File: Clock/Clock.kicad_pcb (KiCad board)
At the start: 2 copper layers, 85 x 100 mm, 49 parts, among them J1 LED, J2 BUS LEDs, J3 USB_B_Micro, SW1 Pulse, SW2 SW_SPDT, SW3 Reset, U1 TLC555xP, U2 TLC555xP, U3 TLC555xP, U4 74HC14, U5 74LS08, U6 74LS32

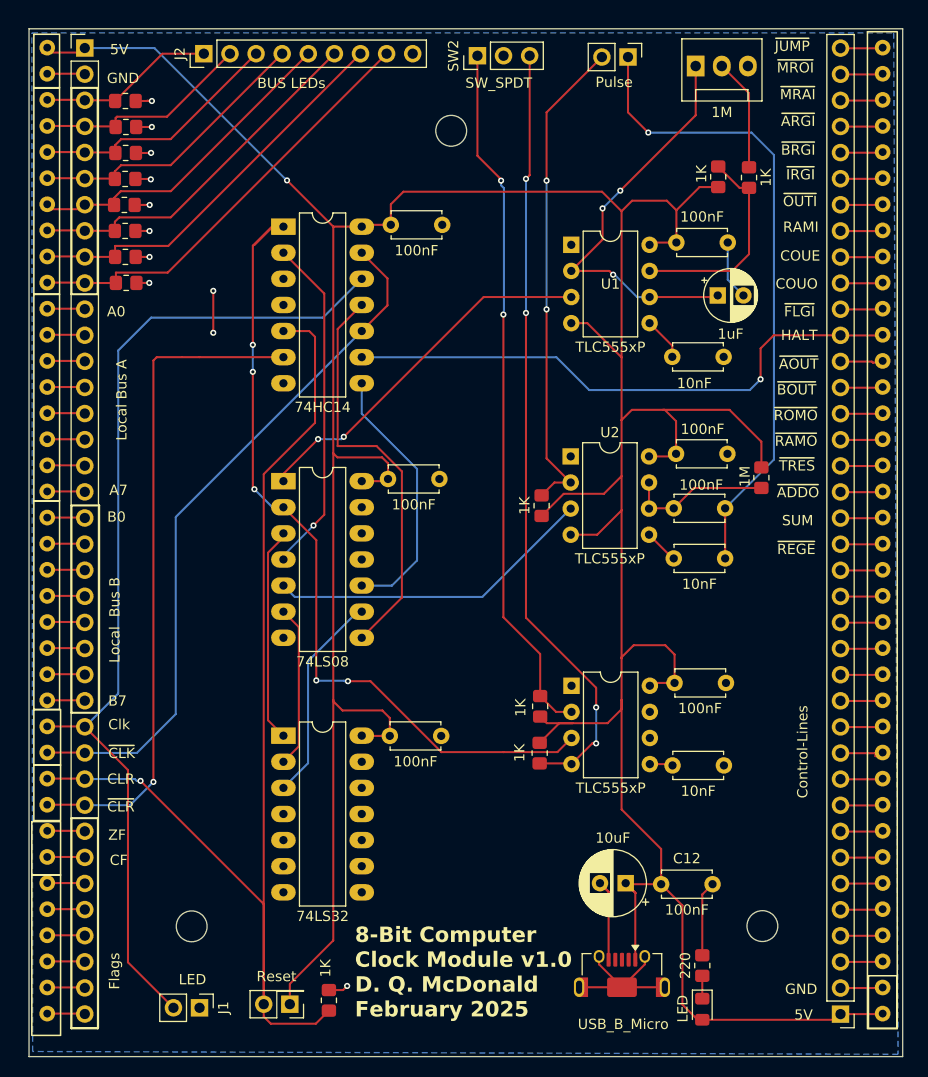
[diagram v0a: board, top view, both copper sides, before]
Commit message: Template PCB size adjustment
Keeping it within the PCBWay $5 size
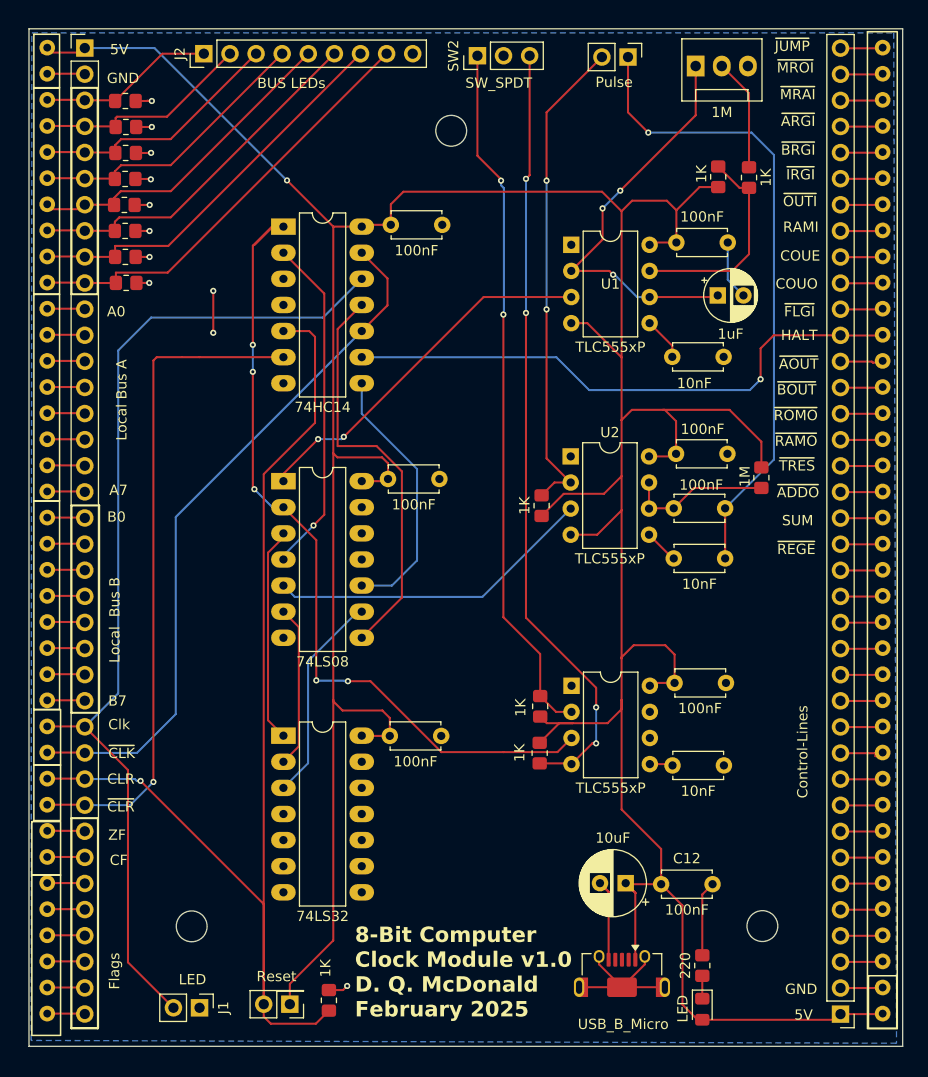
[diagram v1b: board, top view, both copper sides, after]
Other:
- board size 85 x 100 mm -> 85 x 99 mm
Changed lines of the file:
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@@
 	(gr_rect
 		(start 23.85 29.425)
-		(end 108.85 129.425)
+		(end 108.85 128.425)
 		(stroke
 			(width 0.05)
@@
 		(polygon
 			(pts
-				(xy 107.975 29.825) (xy 108.4 129.2) (xy 24.2 128.925) (xy 24.125 29.825)
+				(xy 107.975 29.825) (xy 108.25 128.125) (xy 24.05 127.85) (xy 24.125 29.825)
 			)
 		)

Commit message: Initial version of Registers Schematic
Essentially complete and has footprints.
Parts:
- added R17: 2K, Resistor_SMD:R_0805_2012Metric_Pad1.20x1.40mm_HandSolder, F.Cu at (65.4, 67.5)
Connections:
- C6 pad 2: Net-(C6-Pad2) -> GND
- C7 pad 2: Net-(C6-Pad2) -> GND
- SW1 pad 1: Net-(C6-Pad2) -> GND
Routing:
- net GND: track 50.3 -> 118.3 mm, vias 11 -> 12
- net Net-(C6-Pad2): track 62.5 -> 0.00 mm, vias 1 -> 0
- net unconnected-(J3-Shield-Pad6)_5: track 15.3 -> 0.00 mm
- net unconnected-(J3-Shield-Pad6)_1: track 0.00 -> 15.3 mm
- net HALT: track 55.7 -> 61.2 mm, vias 1 -> 2
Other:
- board text added: "8-Bit Computer Clock Module v1.1 D. Q. McDonald February 2025"
- board text removed: "8-Bit Computer Clock Module v1.0 D. Q. McDonald February 2025"

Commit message: Updated to v2.0. Sent to manufacturing after review.
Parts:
- removed J3: USB_B_Micro, Connector_USB:USB_Micro-AB_Molex_47590-0001
- removed REF** (x3): MountingHole_3mm, MountingHole:MountingHole_3mm
- added C14: .33uF, Capacitor_THT:CP_Radial_D5.0mm_P2.50mm, F.Cu at (66.3, 119.7)
- added J4: DC Input 12V Max, Connector_BarrelJack:BarrelJack_Horizontal, F.Cu at (85.3, 113.5)
- added U7: LM7805_TO220, Package_TO_SOT_THT:TO-220-3_Vertical, F.Cu at (74.7, 117.0)
- moved C11 16.0 mm to (66.2, 109.3)
- moved C12 15.8 mm to (71.2, 105.7)
- moved D1 8.64 mm to (95.5, 118.8)
- moved R16 8.64 mm to (95.5, 114.5)
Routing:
- net 5V: track 368.5 -> 531.1 mm, vias 1 -> 4
- net Net-(U7-VI): track 0.00 -> 21.9 mm
- net unconnected-(J3-Shield-Pad6)_1: track 15.3 -> 0.00 mm
- net GND: track 118.3 -> 110.0 mm, vias 12 -> 10
- net ~{CLOCK}: track 68.8 -> 70.5 mm, vias 0 -> 2
- net CLOCK: track 99.4 -> 99.8 mm, vias 0 -> 1
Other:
- board size 85 x 99 mm -> 86.2 x 99.9 mm
- board text added: "8-Bit Computer Clock Module v2.0 D. Q. McDonald May 2026"
- board text removed: "8-Bit Computer Clock Module v1.1 D. Q. McDonald February 2025"
